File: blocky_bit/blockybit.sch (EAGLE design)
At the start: 98 parts, among them IC2 PAM8301, IC4 LIS3DH, U1 ESP-WROOM-32, U2 AP2112-3.3, U3 ATMEGA32U4, X1 JSTPH, Y2 16MHz

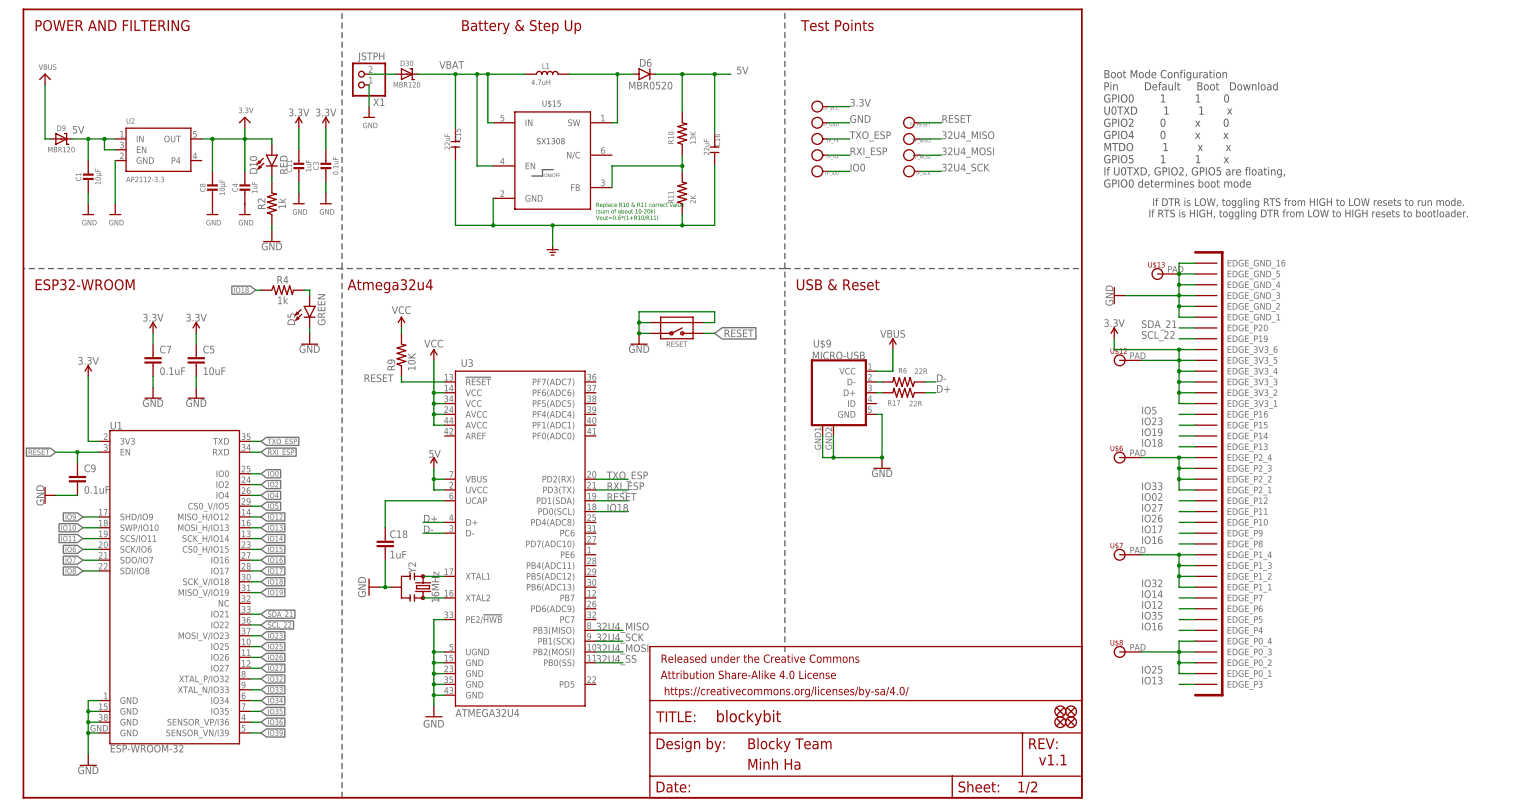
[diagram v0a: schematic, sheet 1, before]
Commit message: Update new layout for blockybit
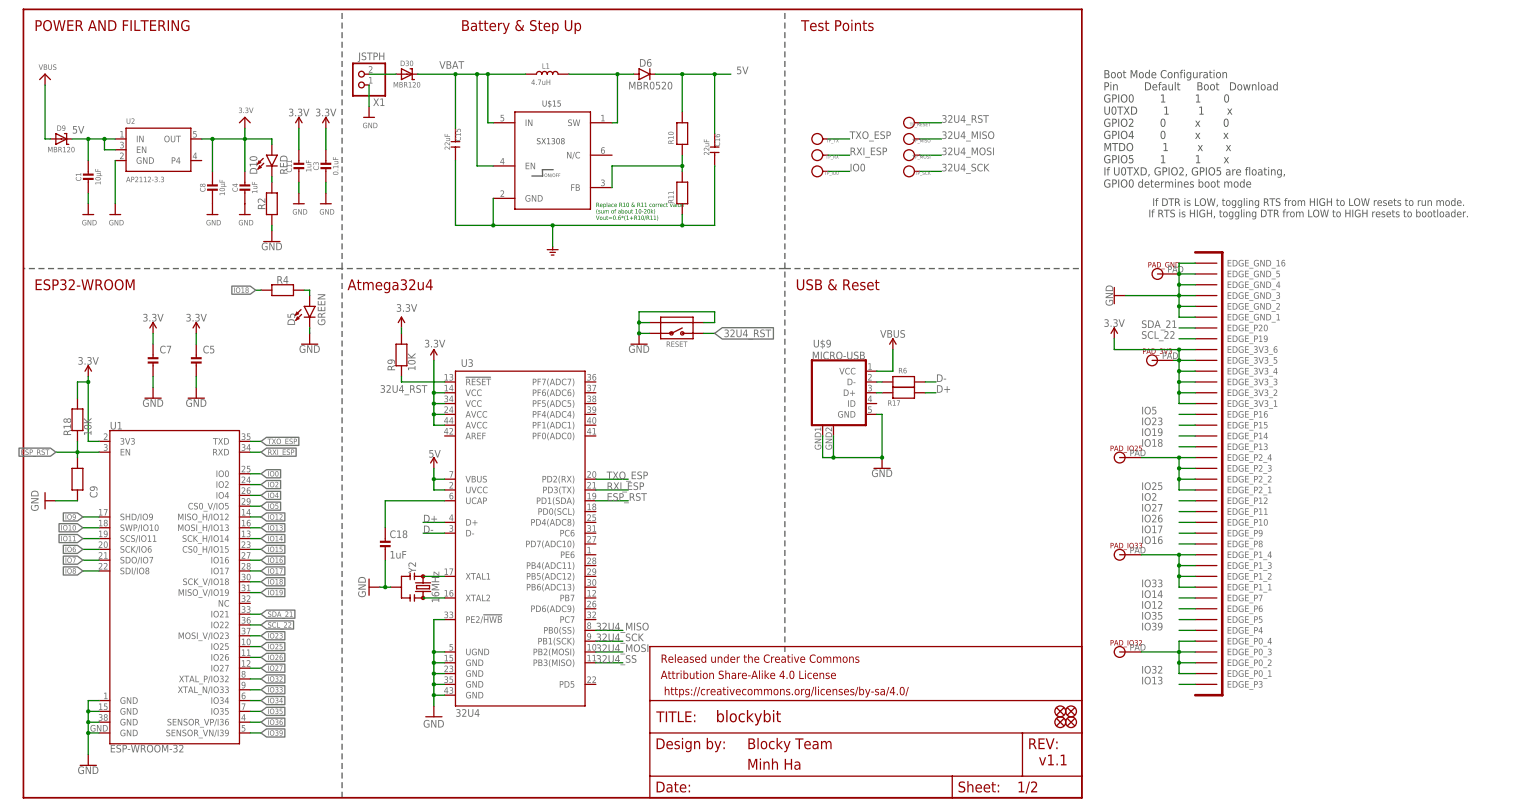
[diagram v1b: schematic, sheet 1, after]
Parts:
- removed R16: 11K, microbuilder:RESISTOR_0603
- removed RIGHT_LIGHT_SENSOR: (no value), microbuilder:LED0805
- removed TP_GND, TP_VCC: (no value), Discrete:PAD-TEST-POINT'3535'
- removed U$12: MICROBIT_PADMICROBIT_PAD_SMALL, microbit:MICROBIT_PADMICROBIT_PAD_SMALL
- added PAD_3V3: MICROBIT_PADMICROBIT_PAD_SMALL, microbit:MICROBIT_PADMICROBIT_PAD_SMALL
- added R18: 10K, microbuilder:RESISTOR_0603
- C14, C17: device SparkFun-Capacitors:0.1UF-0603-25V-5% -> microbuilder:CAP_CERAMIC_0603
- C18: device SparkFun:CAP0603-CAP -> microbuilder:CAP_CERAMIC_0603
- C5: device SparkFun-Capacitors:10UF-0603-6.3V-20% -> microbuilder:CAP_CERAMIC_0603
- C7: device SparkFun-Capacitors:0.1UF-0603-25V-(+80/-20%) -> microbuilder:CAP_CERAMIC_0603
- C9: device SparkFun-Capacitors:0.1UF-0603-25V-(+80/-20%) -> microbuilder:RESISTOR_0603
- R1, R12, R13, R14, R2, R4: device SparkFun-Resistors:1KOHM-0603-1/10W-1% -> microbuilder:RESISTOR_0603
- R10, R11, R17, R6, R8: device SparkFun-Resistors:RESISTOR0603 -> microbuilder:RESISTOR_0603
- R9: device SparkFun:RESISTOR0603-RES -> microbuilder:RESISTOR_0603
- RGB1, RGB10, RGB11, RGB12, RGB13, RGB14, RGB15, RGB16, RGB17, RGB18, RGB19, RGB2, RGB20, RGB21, RGB22, RGB23, RGB24, RGB25, RGB3, RGB4, RGB5, RGB6, RGB7, RGB8, RGB9: device SparkFun-LED:WS2812B -> Blocky:WS2812BWS2812B-3535
- U3: value ATMEGA32U4 -> 32U4; device Testing:ATMEGA32U4OUTFAKES -> SparkFun-IC-Microcontroller:ATMEGA32U4QFN
- renumbered LEFT_LIGHT_SENSOR to LIGHT_SENSOR, U$13 to PAD_GND, U$6 to PAD_IO25, U$7 to PAD_IO33, U$8 to PAD_IO32
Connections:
- removed net IO02: U$1.EDGE_P12
- removed net N$30: C18.2, U3.UCAP
- removed net RESET: C9.1, R9.1, RESET.2, TP_RESET.T, U1.EN, U3.!RESET, U3.PD1(SDA)
- removed net VCC: R9.2, U3.AVCC@24, U3.AVCC@44, U3.VCC@14, U3.VCC@34
- new net 32U4_RST: R9.1, RESET.2, TP_RESET.T, U3.!RESET
- new net ESP_RST: C9.1, R18.1, U1.EN, U3.PD1(SDA)
- new net UCAP: C18.P$2, U3.UCAP
- net 3.3V: now also C5.P$1, C7.P$1, PAD_3V3.P$1, R18.2, R9.2, U3.AVCC@24, U3.AVCC@44, U3.VCC@14, U3.VCC@34; no longer C5.1, C7.1, RIGHT_LIGHT_SENSOR.A, TP_VCC.T, U$12.P$1
- net 32U4_MISO: now also U3.PB0(SS); no longer U3.PB3(MISO)
- net 32U4_SS: now also U3.PB3(MISO); no longer U3.PB0(SS)
- net GND: now also C14.P$2, C17.P$2, C18.P$1, C5.P$2, C7.P$2, RGB14.VSS; no longer C14.2, C17.2, C18.1, C5.2, C7.2, R16.1, TP_GND.T
- net IO16: no longer U$1.EDGE_P4
- net IO18: no longer U3.PD0(SCL)
- net IO2: now also U$1.EDGE_P12
- net IO25: now also PAD_IO25.P$1, U$1.EDGE_P2_1, U$1.EDGE_P2_2, U$1.EDGE_P2_3, U$1.EDGE_P2_4; no longer PAD_IO32.P$1, U$1.EDGE_P0_1, U$1.EDGE_P0_2, U$1.EDGE_P0_3, U$1.EDGE_P0_4
- net IO27: now also C17.P$1; no longer C17.1
- net IO32: now also PAD_IO32.P$1, U$1.EDGE_P0_1, U$1.EDGE_P0_2, U$1.EDGE_P0_3, U$1.EDGE_P0_4; no longer PAD_IO33.P$1, U$1.EDGE_P1_1, U$1.EDGE_P1_2, U$1.EDGE_P1_3, U$1.EDGE_P1_4
- net IO33: now also PAD_IO33.P$1, U$1.EDGE_P1_1, U$1.EDGE_P1_2, U$1.EDGE_P1_3, U$1.EDGE_P1_4; no longer PAD_IO25.P$1, U$1.EDGE_P2_1, U$1.EDGE_P2_2, U$1.EDGE_P2_3, U$1.EDGE_P2_4
- net IO35: now also C14.P$1; no longer C14.1
- net IO39: now also U$1.EDGE_P4; no longer R16.2, RIGHT_LIGHT_SENSOR.C
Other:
- moved on the sheet: C9
